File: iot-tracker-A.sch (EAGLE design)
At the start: 31 parts, among them Q1 MMBT3906, U1 ESP-WROOM-02, U2 TPS61021ADSGR, U3 PCF85263ATL_AX, Y1 32.768kHz

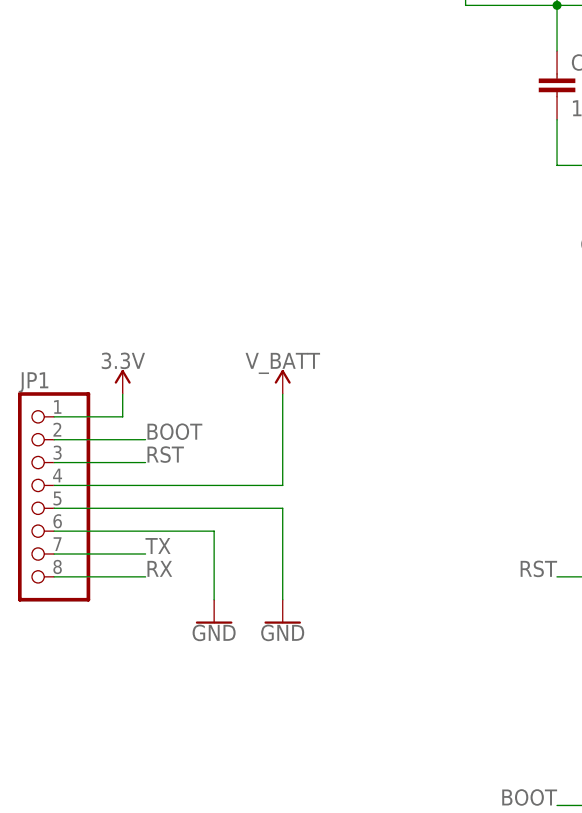
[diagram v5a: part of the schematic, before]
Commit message: Replaced 1x8 header with buttons, screw terminals, and a 1x4 header
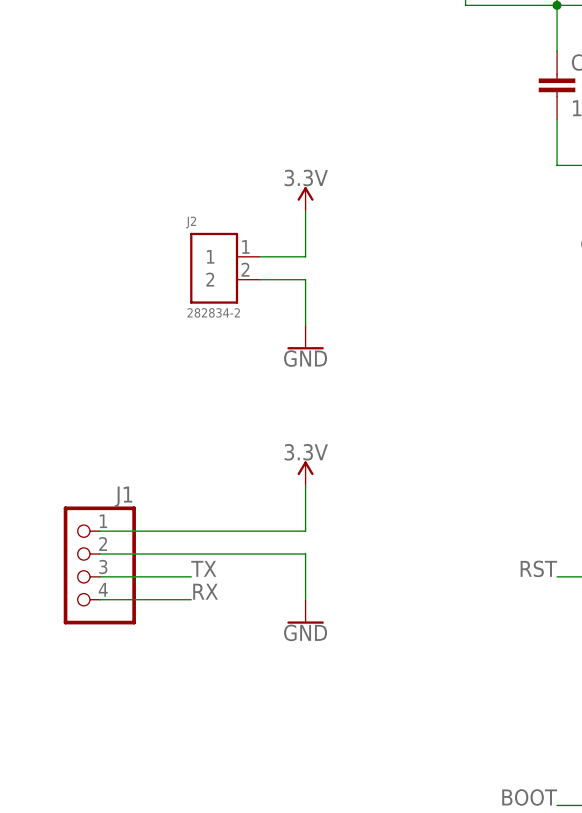
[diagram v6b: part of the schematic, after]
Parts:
- removed JP1: (no value), pinhead:PINHD-1X8
- added J1: (no value), pinhead:PINHD-1X4
- added J2: 282834-2, IOT-Tracker-A:282834-2
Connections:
- net 3.3V: now also J1.1, J2.1; no longer JP1.1
- net BOOT: no longer JP1.2
- net GND: now also J1.2, J2.2; no longer JP1.5, JP1.6
- net RST: no longer JP1.3
- net RX: now also J1.4; no longer JP1.8
- net TX: now also J1.3; no longer JP1.7
- net V_BATT: no longer JP1.4
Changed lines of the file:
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@@
 <part name="D1" library="SparkFun-LED" library_urn="urn:adsk.eagle:library:529" deviceset="LED-GREEN" device="0603" package3d_urn="urn:adsk.eagle:package:39354/1" value="GREEN"/>
 <part name="SUPPLY5" library="SparkFun-PowerSymbols" library_urn="urn:adsk.eagle:library:530" deviceset="3.3V" device=""/>
-<part name="JP1" library="pinhead" library_urn="urn:adsk.eagle:library:325" deviceset="PINHD-1X8" device="" package3d_urn="urn:adsk.eagle:package:22409/2"/>
-<part name="SUPPLY8" library="SparkFun-PowerSymbols" library_urn="urn:adsk.eagle:library:530" deviceset="3.3V" device=""/>
-<part name="SUPPLY9" library="SparkFun-PowerSymbols" library_urn="urn:adsk.eagle:library:530" deviceset="V_BATT" device=""/>
-<part name="GND11" library="SparkFun-PowerSymbols" library_urn="urn:adsk.eagle:library:530" deviceset="GND" device=""/>
-<part name="GND1" library="SparkFun-PowerSymbols" library_urn="urn:adsk.eagle:library:530" deviceset="GND" device=""/>
 <part name="U2" library="IOT-Tracker-A" deviceset="TPS61021ADSGR" device=""/>
 <part name="SUPPLY6" library="SparkFun-PowerSymbols" library_urn="urn:adsk.eagle:library:530" deviceset="V_BATT" device=""/>
@@
 <part name="R11" library="SparkFun-Resistors" library_urn="urn:adsk.eagle:library:532" deviceset="10KOHM" device="-0603-1/10W-1%" package3d_urn="urn:adsk.eagle:package:39650/1" value="10k"/>
 <part name="SUPPLY11" library="SparkFun-PowerSymbols" library_urn="urn:adsk.eagle:library:530" deviceset="3.3V" device=""/>
+<part name="J1" library="pinhead" library_urn="urn:adsk.eagle:library:325" deviceset="PINHD-1X4" device="" package3d_urn="urn:adsk.eagle:package:22407/2"/>
+<part name="SUPPLY8" library="SparkFun-PowerSymbols" library_urn="urn:adsk.eagle:library:530" deviceset="3.3V" device=""/>
+<part name="GND1" library="SparkFun-PowerSymbols" library_urn="urn:adsk.eagle:library:530" deviceset="GND" device=""/>
+<part name="SUPPLY9" library="SparkFun-PowerSymbols" library_urn="urn:adsk.eagle:library:530" deviceset="3.3V" device=""/>
+<part name="GND11" library="SparkFun-PowerSymbols" library_urn="urn:adsk.eagle:library:530" deviceset="GND" device=""/>
+<part name="J2" library="IOT-Tracker-A" deviceset="282834-2" device=""/>
 </parts>
 <sheets>
@@
 <attribute name="VALUE" x="33.02" y="0.254" size="1.778" layer="96" align="bottom-center"/>
 </instance>
-<instance part="JP1" gate="A" x="-134.62" y="-25.4" smashed="yes" rot="MR0">
-<attribute name="NAME" x="-135.89" y="-12.065" size="1.778" layer="95"/>
-<attribute name="VALUE" x="-128.27" y="-38.1" size="1.778" layer="96" rot="MR0"/>
-</instance>
-<instance part="SUPPLY8" gate="G$1" x="-124.46" y="-12.7" smashed="yes" rot="MR0">
-<attribute name="VALUE" x="-124.46" y="-9.906" size="1.778" layer="96" rot="MR0" align="bottom-center"/>
-</instance>
-<instance part="SUPPLY9" gate="G$1" x="-106.68" y="-12.7" smashed="yes" rot="MR0">
-<attribute name="VALUE" x="-106.68" y="-9.906" size="1.778" layer="96" rot="MR0" align="bottom-center"/>
-</instance>
-<instance part="GND11" gate="1" x="-114.3" y="-38.1" smashed="yes">
-<attribute name="VALUE" x="-114.3" y="-38.354" size="1.778" layer="96" align="top-center"/>
-</instance>
-<instance part="GND1" gate="1" x="-106.68" y="-38.1" smashed="yes">
-<attribute name="VALUE" x="-106.68" y="-38.354" size="1.778" layer="96" align="top-center"/>
-</instance>
 <instance part="U2" gate="G$1" x="-60.96" y="48.26" smashed="yes">
 <attribute name="NAME" x="-54.61" y="55.88" size="1.778" layer="95" align="center-left"/>
@@
 <instance part="SUPPLY11" gate="G$1" x="-68.58" y="-43.18" smashed="yes" rot="MR0">
 <attribute name="VALUE" x="-68.58" y="-40.386" size="1.778" layer="96" rot="MR0" align="bottom-center"/>
+</instance>
+<instance part="J1" gate="A" x="-129.54" y="-33.02" smashed="yes" rot="MR0">
+<attribute name="NAME" x="-123.19" y="-24.765" size="1.778" layer="95" rot="MR0"/>
+<attribute name="VALUE" x="-123.19" y="-40.64" size="1.778" layer="96" rot="MR0"/>
+</instance>
+<instance part="SUPPLY8" gate="G$1" x="-104.14" y="-22.86" smashed="yes" rot="MR0">
+<attribute name="VALUE" x="-104.14" y="-20.066" size="1.778" layer="96" rot="MR0" align="bottom-center"/>
+</instance>
+<instance part="GND1" gate="1" x="-104.14" y="-38.1" smashed="yes">
+<attribute name="VALUE" x="-104.14" y="-38.354" size="1.778" layer="96" align="top-center"/>
+</instance>
+<instance part="SUPPLY9" gate="G$1" x="-104.14" y="7.62" smashed="yes" rot="MR0">
+<attribute name="VALUE" x="-104.14" y="10.414" size="1.778" layer="96" rot="MR0" align="bottom-center"/>
+</instance>
+<instance part="GND11" gate="1" x="-104.14" y="-7.62" smashed="yes">
+<attribute name="VALUE" x="-104.14" y="-7.874" size="1.778" layer="96" align="top-center"/>
+</instance>
+<instance part="J2" gate="G$1" x="-114.3" y="2.54" smashed="yes">
+<attribute name="NAME" x="-117.35226875" y="5.973809375" size="1.01741875" layer="95"/>
+<attribute name="VALUE" x="-117.35121875" y="-4.1981" size="1.01706875" layer="96"/>
 </instance>
 </instances>
@@
 </segment>
 <segment>
-<pinref part="JP1" gate="A" pin="6"/>
-<wire x1="-132.08" y1="-27.94" x2="-114.3" y2="-27.94" width="0.1524" layer="91"/>
-<wire x1="-114.3" y1="-27.94" x2="-114.3" y2="-35.56" width="0.1524" layer="91"/>
-<pinref part="GND11" gate="1" pin="GND"/>
-</segment>
-<segment>
-<pinref part="JP1" gate="A" pin="5"/>
-<pinref part="GND1" gate="1" pin="GND"/>
-<wire x1="-132.08" y1="-25.4" x2="-106.68" y2="-25.4" width="0.1524" layer="91"/>
-<wire x1="-106.68" y1="-25.4" x2="-106.68" y2="-35.56" width="0.1524" layer="91"/>
-</segment>
-<segment>
 <pinref part="U2" gate="G$1" pin="PGND"/>
 <pinref part="GND10" gate="1" pin="GND"/>
@@
 <pinref part="GND16" gate="1" pin="GND"/>
 </segment>
+<segment>
+<pinref part="J1" gate="A" pin="2"/>
+<wire x1="-127" y1="-30.48" x2="-104.14" y2="-30.48" width="0.1524" layer="91"/>
+<wire x1="-104.14" y1="-30.48" x2="-104.14" y2="-35.56" width="0.1524" layer="91"/>
+<pinref part="GND1" gate="1" pin="GND"/>
+</segment>
+<segment>
+<pinref part="J2" gate="G$1" pin="2"/>
+<pinref part="GND11" gate="1" pin="GND"/>
+<wire x1="-109.22" y1="0" x2="-104.14" y2="0" width="0.1524" layer="91"/>
+<wire x1="-104.14" y1="0" x2="-104.14" y2="-5.08" width="0.1524" layer="91"/>
+</segment>
 </net>
 <net name="IO15" class="2">
@@
 </segment>
 <segment>
-<pinref part="JP1" gate="A" pin="8"/>
-<wire x1="-132.08" y1="-33.02" x2="-121.92" y2="-33.02" width="0.1524" layer="91"/>
-<label x="-121.92" y="-33.02" size="1.778" layer="95"/>
+<pinref part="J1" gate="A" pin="4"/>
+<wire x1="-127" y1="-35.56" x2="-116.84" y2="-35.56" width="0.1524" layer="91"/>
+<label x="-116.84" y="-35.56" size="1.778" layer="95"/>
 </segment>
 </net>
@@
 </segment>
 <segment>
-<pinref part="JP1" gate="A" pin="7"/>
-<wire x1="-132.08" y1="-30.48" x2="-121.92" y2="-30.48" width="0.1524" layer="91"/>
-<label x="-121.92" y="-30.48" size="1.778" layer="95"/>
+<pinref part="J1" gate="A" pin="3"/>
+<wire x1="-127" y1="-33.02" x2="-116.84" y2="-33.02" width="0.1524" layer="91"/>
+<label x="-116.84" y="-33.02" size="1.778" layer="95"/>
 </segment>
 </net>
@@
 <wire x1="43.18" y1="-48.26" x2="50.8" y2="-48.26" width="0.1524" layer="91"/>
 <label x="50.8" y="-48.26" size="1.778" layer="95"/>
-</segment>
-<segment>
-<pinref part="JP1" gate="A" pin="2"/>
-<wire x1="-132.08" y1="-17.78" x2="-121.92" y2="-17.78" width="0.1524" layer="91"/>
-<label x="-121.92" y="-17.78" size="1.778" layer="95"/>
 </segment>
 <segment>
@@
 <pinref part="C3" gate="G$1" pin="+"/>
 <wire x1="66.04" y1="-15.24" x2="53.34" y2="-15.24" width="0.1524" layer="91"/>
-</segment>
-<segment>
-<pinref part="JP1" gate="A" pin="1"/>
-<wire x1="-132.08" y1="-15.24" x2="-124.46" y2="-15.24" width="0.1524" layer="91"/>
-<wire x1="-124.46" y1="-15.24" x2="-124.46" y2="-12.7" width="0.1524" layer="91"/>
-<pinref part="SUPPLY8" gate="G$1" pin="3.3V"/>
 </segment>
 <segment>
@@
 <wire x1="-68.58" y1="-45.72" x2="-68.58" y2="-43.18" width="0.1524" layer="91"/>
 </segment>
+<segment>
+<pinref part="J1" gate="A" pin="1"/>
+<wire x1="-127" y1="-27.94" x2="-104.14" y2="-27.94" width="0.1524" layer="91"/>
+<wire x1="-104.14" y1="-27.94" x2="-104.14" y2="-22.86" width="0.1524" layer="91"/>
+<pinref part="SUPPLY8" gate="G$1" pin="3.3V"/>
+</segment>
+<segment>
+<pinref part="J2" gate="G$1" pin="1"/>
+<pinref part="SUPPLY9" gate="G$1" pin="3.3V"/>
+<wire x1="-109.22" y1="2.54" x2="-104.14" y2="2.54" width="0.1524" layer="91"/>
+<wire x1="-104.14" y1="2.54" x2="-104.14" y2="7.62" width="0.1524" layer="91"/>
+</segment>
 </net>
 <net name="V_BATT" class="1">
-<segment>
-<pinref part="SUPPLY9" gate="G$1" pin="V_BATT"/>
-<pinref part="JP1" gate="A" pin="4"/>
-<wire x1="-106.68" y1="-12.7" x2="-106.68" y2="-22.86" width="0.1524" layer="91"/>
-<wire x1="-106.68" y1="-22.86" x2="-132.08" y2="-22.86" width="0.1524" layer="91"/>
-</segment>
 <segment>
 <pinref part="U2" gate="G$1" pin="VIN"/>
@@
 </segment>
 <segment>
-<pinref part="JP1" gate="A" pin="3"/>
-<wire x1="-132.08" y1="-20.32" x2="-121.92" y2="-20.32" width="0.1524" layer="91"/>
-<label x="-121.92" y="-20.32" size="1.778" layer="95"/>
-</segment>
-<segment>

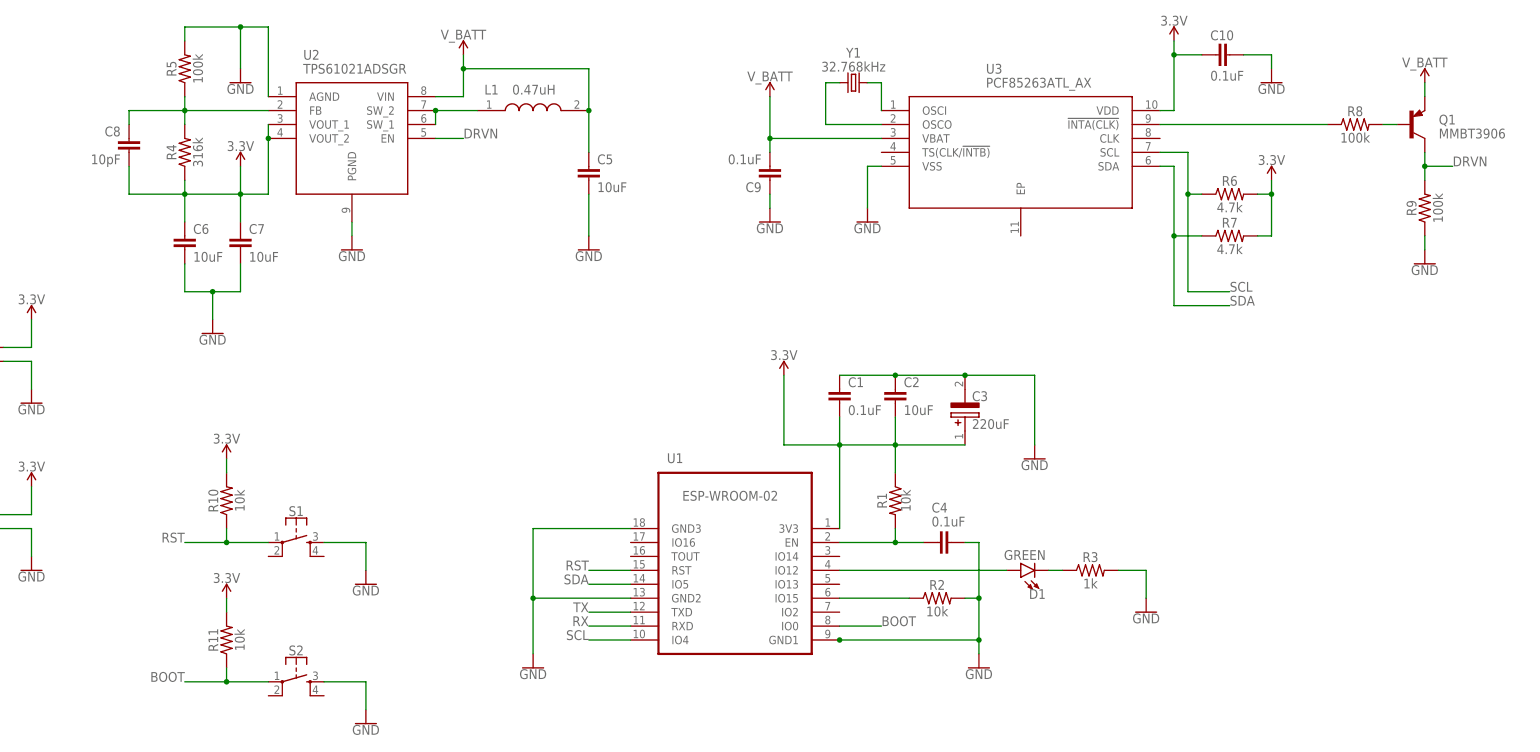
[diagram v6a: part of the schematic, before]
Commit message: Connected a MOSFET switch and voltage divider to the ADC; connected a capacitor to boost enable pin
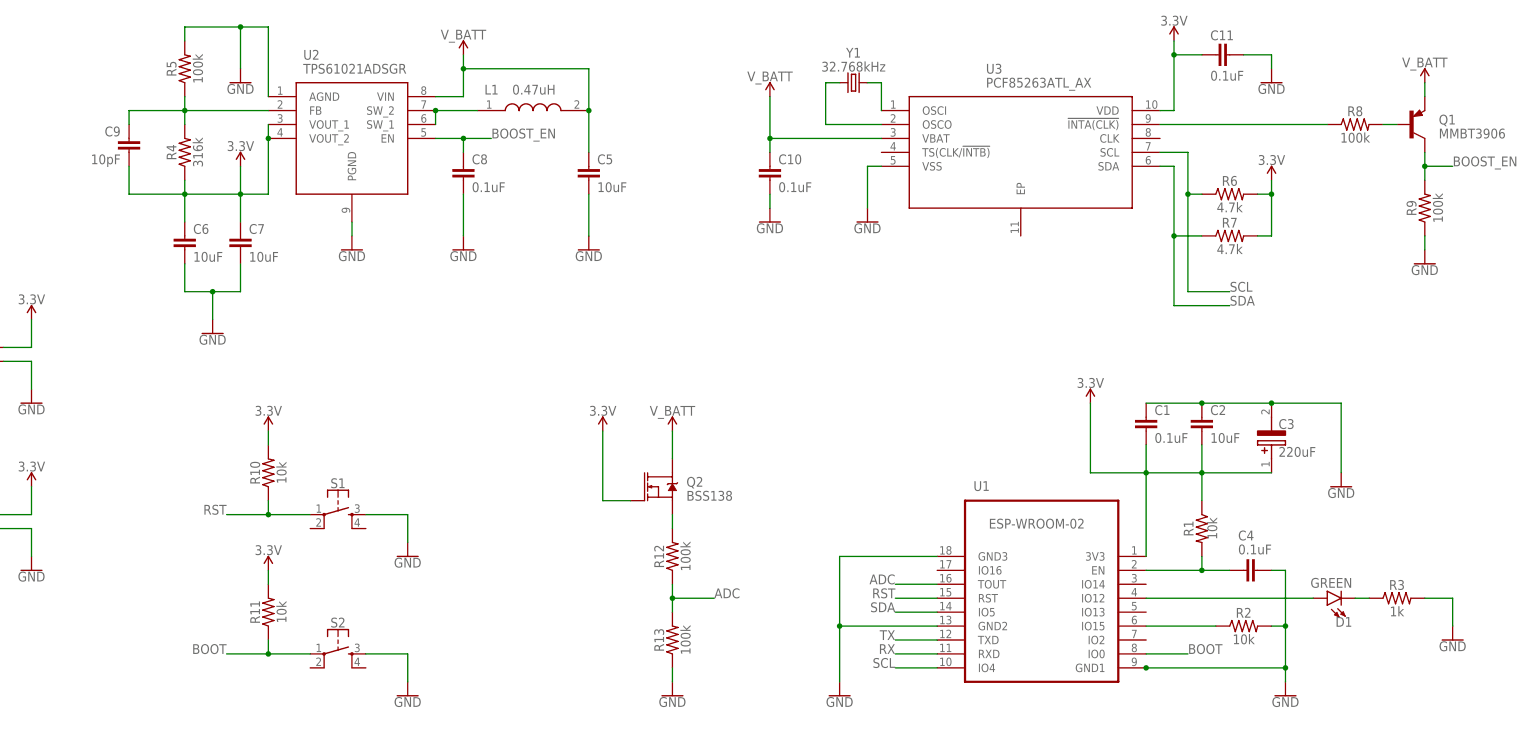
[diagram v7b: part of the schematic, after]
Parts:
- added C11: 0.1uF, SparkFun-Capacitors:0.1UF-0603-25V-(+80/-20%)
- added Q2: BSS138, SparkFun-DiscreteSemi:MOSFET-NCH-BSS138
- added R12, R13: 100k, SparkFun-Resistors:100KOHM-0603-1/10W-1%
- C8: value 10pF -> 0.1uF; device SparkFun-Capacitors:10PF-0603-50V-5% -> SparkFun-Capacitors:0.1UF-0603-25V-(+80/-20%)
- C9: value 0.1uF -> 10pF; device SparkFun-Capacitors:0.1UF-0603-25V-(+80/-20%) -> SparkFun-Capacitors:10PF-0603-50V-5%
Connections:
- net EN renamed ESP_EN
- removed net DRVN: Q1.C, R9.2, U2.EN
- new net ADC: R12.1, R13.2, U1.TOUT
- new net BOOST_EN: C8.1, Q1.C, R9.2, U2.EN
- new net N$1: Q2.S, R12.2
- net 3.3V: now also C11.2, C9.2, Q2.G; no longer C10.2, C8.2
- net FB: now also C9.1; no longer C8.1
- net GND: now also C10.2, C11.1, C8.2, R13.1; no longer C10.1, C9.1
- net V_BATT: now also C10.1, Q2.D; no longer C9.2
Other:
- moved on the sheet: C1, C10, C2, C3, C4, C8, C9, D1, R1, R10, R11, R2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

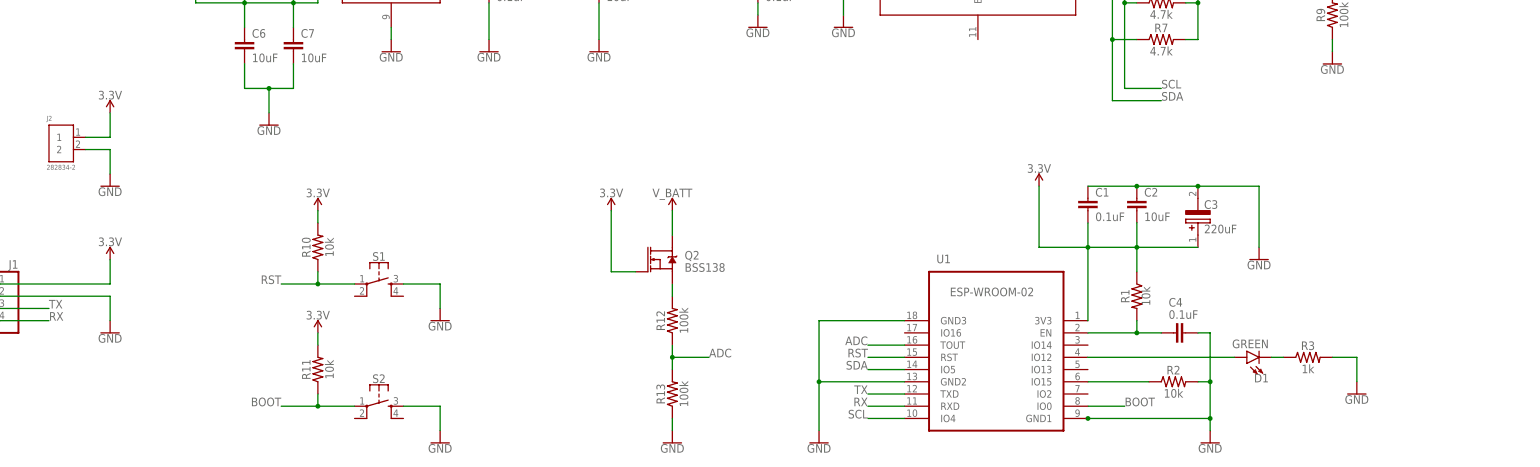
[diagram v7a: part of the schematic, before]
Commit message: Minor net fixes, partially routed every IC
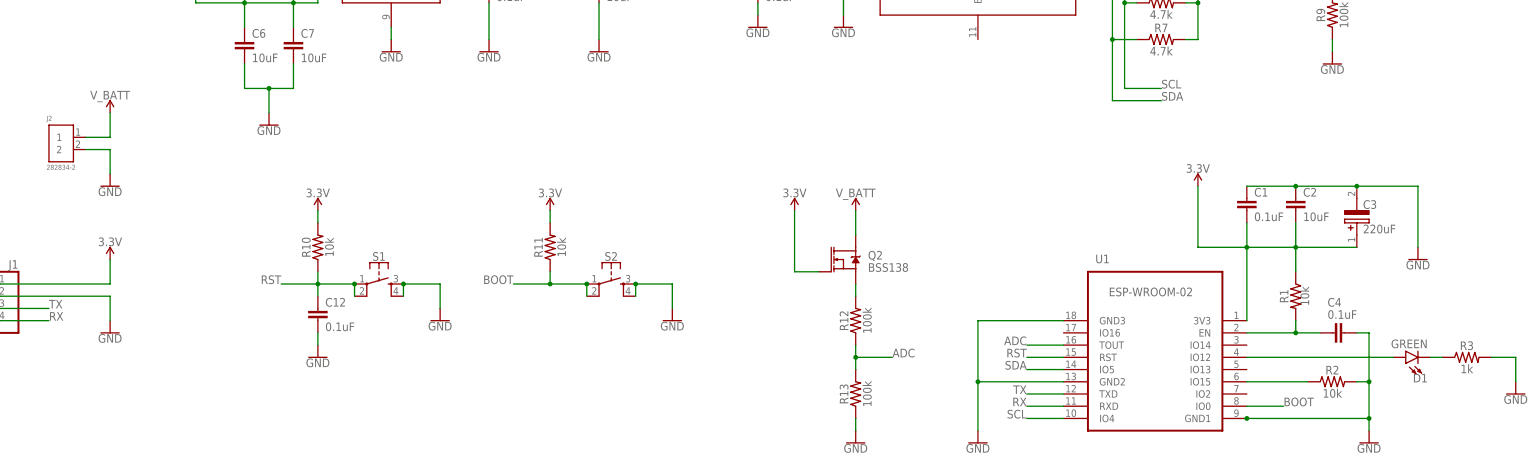
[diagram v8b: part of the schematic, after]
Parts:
- added C12: 0.1uF, SparkFun-Capacitors:0.1UF-0603-25V-(+80/-20%)
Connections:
- net INTA_PNP_B renamed PNP_B
- net N$1 renamed MOSFET_S
- net 3.3V: no longer J2.1
- net BOOT: now also S2.2
- net GND: now also C12.2, S1.4, S2.4
- net RST: now also C12.1, S1.2
- net V_BATT: now also J2.1
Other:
- moved on the sheet: C1, C2, C3, C4, D1, Q2, R1, R11, R12, R13, R2, R3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
